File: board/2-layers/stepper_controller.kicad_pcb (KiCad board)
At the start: 4 copper layers, 99 x 46 mm, 124 parts, among them J201 USB_OTG, P103 CONN_4, P105 CONN_4, P107 CONN_4, P201 UART1, P301 12V_Conn, U101 DRV8825, U102 DRV8825, U103 DRV8825, U104 MAX5713/4/5-TSSOP14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

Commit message: footprint cleanup
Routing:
- net +3.3V: track 70.3 -> 73.8 mm, vias 24 -> 25
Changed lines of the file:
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@@
   (general
     (links 339)
-    (no_connects 33)
-    (area 105.189999 86.249999 204.300001 132.400001)
+    (no_connects 31)
+    (area 89.761974 77.9404 204.300001 135.742001)
     (thickness 1.6002)
     (drawings 71)
-    (tracks 677)
+    (tracks 685)
     (zones 0)
     (modules 124)
@@
     (2 GND mixed hide)
     (1 POWER mixed hide)
-    (0 BOTTOM signal hide)
+    (0 BOTTOM signal)
     (16 B.Adhes user)
     (17 F.Adhes user)
@@
   (segment (start 196 95) (end 193.5 95) (width 0.508) (layer BOTTOM) (net 2))
   (segment (start 197 96) (end 196 95) (width 0.508) (layer BOTTOM) (net 2))
+  (segment (start 132.75 94.74956) (end 132.75 94.35) (width 0.2) (layer TOP) (net 3))
+  (via (at 132.8 94.3) (size 0.6096) (layers TOP BOTTOM) (net 3))
+  (segment (start 132.75 94.35) (end 132.8 94.3) (width 0.2) (layer TOP) (net 3))
+  (segment (start 131.11994 94.74956) (end 132.75 94.74956) (width 0.2) (layer TOP) (net 3) (status 400000))
+  (segment (start 132.75 94.74956) (end 134.10444 94.74956) (width 0.2) (layer TOP) (net 3))
+  (segment (start 134.10444 94.74956) (end 134.112 94.742) (width 0.2) (layer TOP) (net 3) (status C00000))
   (segment (start 121.49842 90.9675) (end 121.49842 88.43258) (width 0.2) (layer TOP) (net 3))
   (segment (start 121.49842 88.43258) (end 121.539 88.392) (width 0.2) (layer TOP) (net 3))
@@
   (via (at 155.8 95.5) (size 0.6096) (layers TOP BOTTOM) (net 9))
   (segment (start 155.2986 96.0014) (end 155.8 95.5) (width 0.1524) (layer TOP) (net 9))
-  (segment (start 119.2175 94.24918) (end 125.99918 94.24918) (width 0.1524) (layer TOP) (net 10))
-  (segment (start 147.2528 94.5028) (end 152.003 94.5028) (width 0.1524) (layer TOP) (net 10))
-  (segment (start 147.25 94.5) (end 147.2528 94.5028) (width 0.1524) (layer TOP) (net 10))
-  (via (at 147.25 94.5) (size 0.6096) (layers TOP BOTTOM) (net 10))
-  (segment (start 129.5 94.5) (end 147.25 94.5) (width 0.1524) (layer BOTTOM) (net 10))
-  (segment (start 129.25 94.25) (end 129.5 94.5) (width 0.1524) (layer BOTTOM) (net 10))
-  (via (at 129.25 94.25) (size 0.6096) (layers TOP BOTTOM) (net 10))
-  (segment (start 128 95.5) (end 129.25 94.25) (width 0.1524) (layer TOP) (net 10))
-  (segment (start 127.25 95.5) (end 128 95.5) (width 0.1524) (layer TOP) (net 10))
+  (segment (start 129.5 94.5) (end 130 95) (width 0.1524) (layer BOTTOM) (net 10))
   (segment (start 125.99918 94.24918) (end 127.25 95.5) (width 0.1524) (layer TOP) (net 10))
+  (segment (start 127.25 95.5) (end 128 95.5) (width 0.1524) (layer TOP) (net 10))
+  (segment (start 128 95.5) (end 129.25 94.25) (width 0.1524) (layer TOP) (net 10))
+  (via (at 129.25 94.25) (size 0.6096) (layers TOP BOTTOM) (net 10))
+  (segment (start 129.25 94.25) (end 129.5 94.5) (width 0.1524) (layer BOTTOM) (net 10))
+  (via (at 147.25 94.5) (size 0.6096) (layers TOP BOTTOM) (net 10))
+  (segment (start 147.25 94.5) (end 147.2528 94.5028) (width 0.1524) (layer TOP) (net 10))
+  (segment (start 152.003 94.5028) (end 147.2528 94.5028) (width 0.1524) (layer TOP) (net 10))
+  (segment (start 125.99918 94.24918) (end 119.2175 94.24918) (width 0.1524) (layer TOP) (net 10))
+  (segment (start 146.75 95) (end 147.25 94.5) (width 0.1524) (layer BOTTOM) (net 10))
+  (segment (start 130 95) (end 146.75 95) (width 0.1524) (layer BOTTOM) (net 10))
   (segment (start 119.2175 94.74956) (end 125.49956 94.74956) (width 0.1524) (layer TOP) (net 11))
   (segment (start 158.1 94.4) (end 158.7 94.4) (width 0.1524) (layer BOTTOM) (net 11))

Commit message: blabla
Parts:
- removed P201: UART1, PIN_ARRAY_4x1
- moved C405 6.05 mm to (154.7, 100.1), turned to 270 degrees
- moved C403 3.40 mm to (154.9, 105.1)
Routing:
- net +1.2V: track 9.16 -> 30.2 mm, vias 3 -> 4
- net GND: track 12.1 -> 20.6 mm
- net /VRF_2: track 47.1 -> 49.5 mm
- net /VRF_1: track 17.8 -> 20.1 mm
- net /VRF_0: track 36.0 -> 36.7 mm

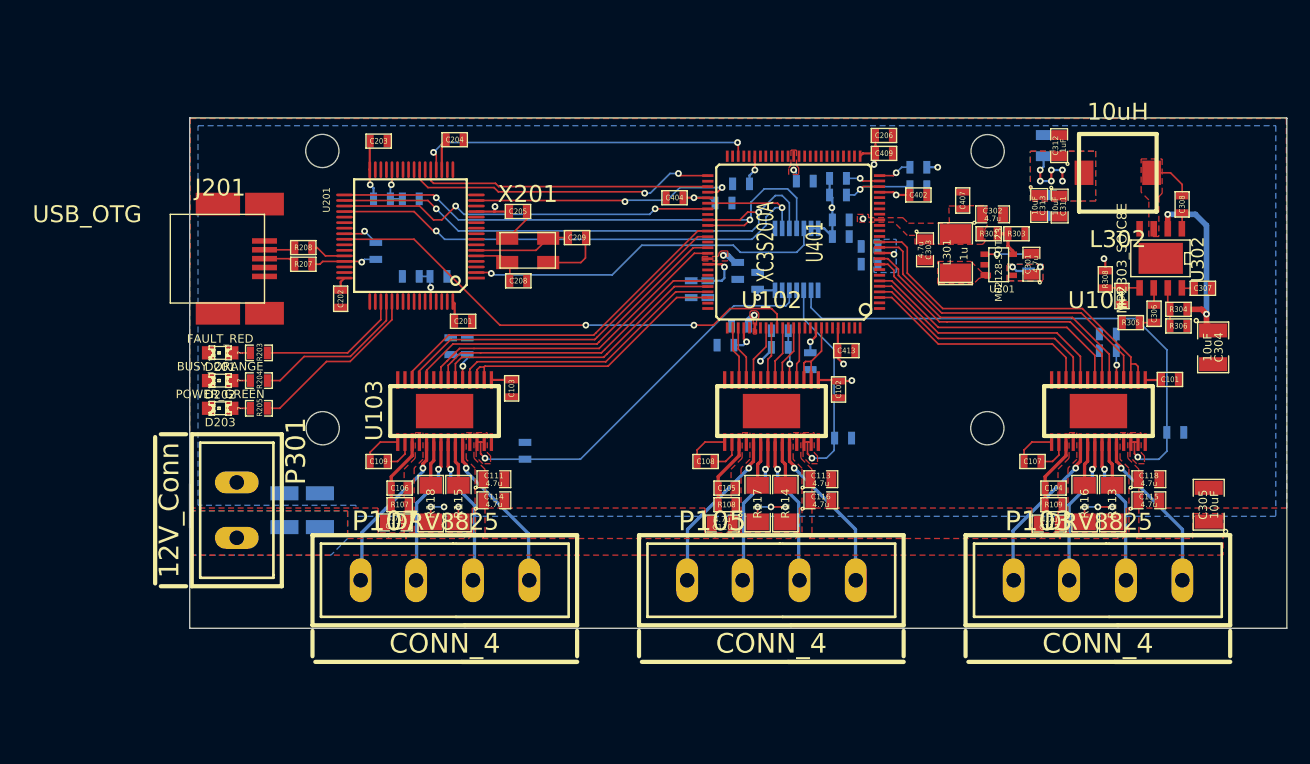
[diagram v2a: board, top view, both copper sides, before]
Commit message: adding mezzanine connector
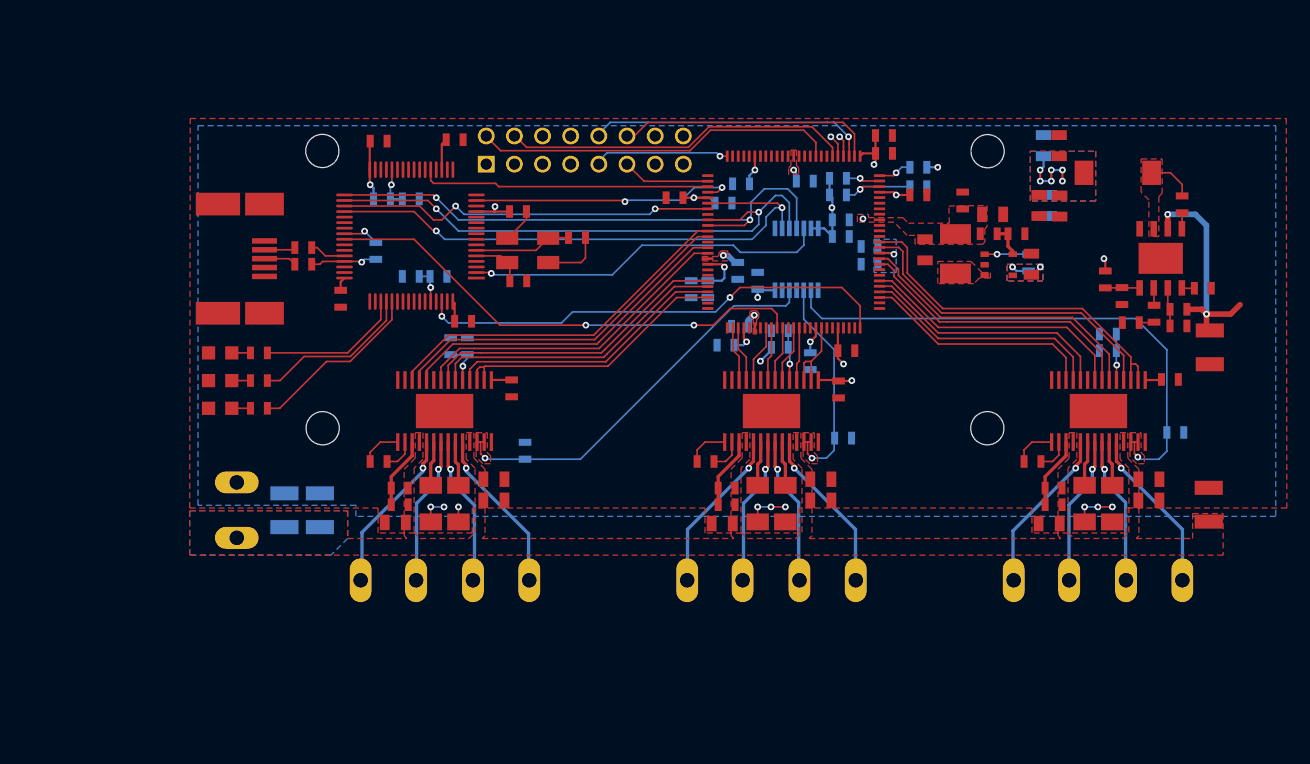
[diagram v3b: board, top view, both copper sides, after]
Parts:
- added P104: CONN_8X2, pin_array_8x2, F.Cu at (140.9, 89.2)
- moved C304 0.30 mm to (197.3, 107.0)
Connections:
- U401 pad 27: (no net) -> /FPGA/L02N
- U401 pad 28: (no net) -> /FPGA/L03P
- U401 pad 29: (no net) -> /FPGA/L03N
- U401 pad 30: (no net) -> /FPGA/L04P
- U401 pad 31: (no net) -> /FPGA/L04N
- U401 pad 34: (no net) -> /FPGA/L06P
- U401 pad 35: (no net) -> /FPGA/L06N
- U401 pad 36: (no net) -> /FPGA/L07P
- U401 pad 37: (no net) -> /FPGA/L07N
- U401 pad 49: (no net) -> /FPGA/L10N
- U401 pad 50: (no net) -> /FPGA/L11P
- U401 pad 52: (no net) -> /FPGA/L11N
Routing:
- net /STM32/FPGA_PROG_B: track 0.00 -> 43.3 mm, vias 0 -> 2
- net /FPGA/L06P: track 0.00 -> 32.8 mm
- net /FPGA/L04N: track 0.00 -> 31.5 mm
- net /STM32/FPGA_INITB: track 30.7 -> 0.00 mm, vias 2 -> 0
- net /FPGA/L04P: track 0.00 -> 29.6 mm, vias 0 -> 1
- net /FPGA/DIN: track 28.2 -> 0.00 mm, vias 2 -> 0
- net /FPGA/L03N: track 0.00 -> 27.3 mm, vias 0 -> 1
- net /FPGA/L03P: track 0.00 -> 25.5 mm, vias 0 -> 1
- net /FPGA/L02N: track 0.00 -> 23.5 mm
- net /FPGA/L11P: track 0.00 -> 12.3 mm, vias 0 -> 1
- net /FPGA/L11N: track 0.00 -> 7.93 mm
- net +12V: track 16.9 -> 20.1 mm
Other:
- board outline removed

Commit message: jtag con & serial
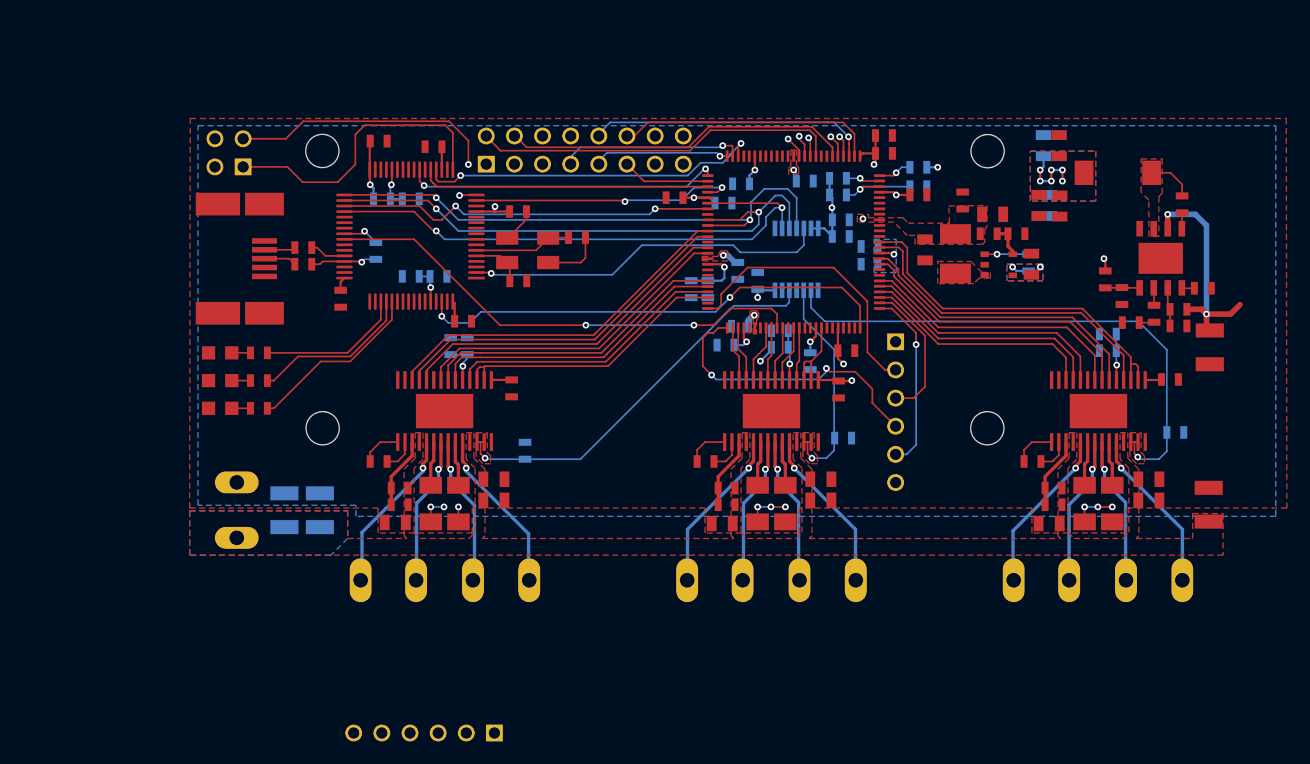
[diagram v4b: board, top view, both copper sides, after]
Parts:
- added P101: JTAG, PIN_ARRAY-6X1, F.Cu at (126.4, 141.8)
- added P102: JTAG, PIN_ARRAY-6X1, F.Cu at (168.9, 112.8)
- added P201: CONN_2X2, PIN_ARRAY_2X2, F.Cu at (108.8, 89.5)
- moved C204 2.01 mm to (127.2, 88.9), turned to 180 degrees
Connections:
- P104 pad 13: +12V -> +3.3V
- P104 pad 14: +3.3V -> GND
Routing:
- net /FPGA/L06N: track 0.00 -> 33.3 mm, vias 0 -> 1
- net /STM32/FPGA_INITB: track 0.00 -> 31.2 mm, vias 0 -> 2
- net /FPGA/L07P: track 0.00 -> 29.1 mm, vias 0 -> 1
- net N-00000127: track 0.00 -> 28.5 mm, vias 0 -> 2
- net /FPGA/DIN: track 0.00 -> 28.4 mm, vias 0 -> 2
- net N-00000115: track 0.00 -> 26.8 mm
- net FPGA_TCK: track 0.00 -> 26.5 mm, vias 0 -> 2
- net /FPGA/L07N: track 0.00 -> 26.4 mm, vias 0 -> 1
- net FPGA_TDO: track 0.00 -> 25.6 mm
- net /FPGA/L10N: track 0.00 -> 16.6 mm, vias 0 -> 1
- net FPGA_TMS: track 0.00 -> 16.5 mm, vias 0 -> 1
- net FPGA_TDI: track 0.00 -> 13.0 mm
- net +3.3V: track 73.8 -> 73.0 mm
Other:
- board text added: "Rx"
- board text added: "TCK"
- board text added: "TDI"
- board text added: "TDO"
- board text added: "TMS"
- board text added: "Tx"

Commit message: routing adc connector + SPI | removed mode selector
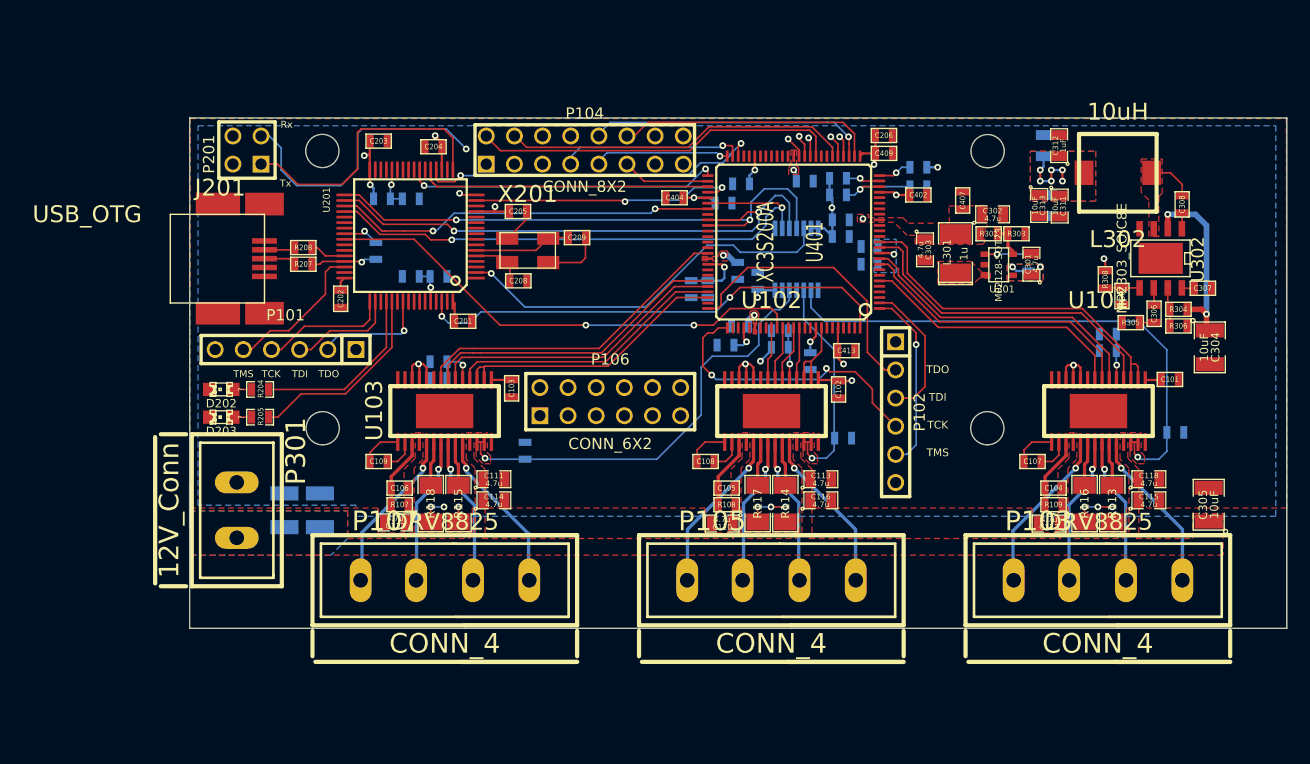
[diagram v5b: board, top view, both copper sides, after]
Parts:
- removed D201: FAULT_RED, LED-0805
- removed R203: ?, SM0603_Resistor
- added P106: CONN_6X2, pin_array_6x2, F.Cu at (143.2, 111.9)
- moved P101 36.8 mm to (113.9, 107.2)
- moved R102 3.89 mm to (127.7, 109.8), turned to 0 degrees
- moved R101 1.78 mm to (127.7, 108.3), turned to 180 degrees
- moved P201 1.64 mm to (110.4, 89.2)
- moved D202 0.81 mm to (108.1, 110.8)
- moved D203 0.81 mm to (108.1, 113.3)
- moved R204 0.81 mm to (111.6, 110.8)
- moved R205 0.81 mm to (111.6, 113.3)
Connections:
- U101 pad 24: /FPGA/M2_MODE0 -> +3.3V
- U101 pad 25: /FPGA/M2_MODE1 -> +3.3V
- U101 pad 26: /FPGA/M2_MODE2 -> +3.3V
- U102 pad 24: /FPGA/M1_MODE0 -> +3.3V
- U102 pad 25: /FPGA/M1_MODE1 -> +3.3V
- U102 pad 26: /FPGA/M1_MODE2 -> +3.3V
- U103 pad 24: /FPGA/M0_MODE0 -> +3.3V
- U103 pad 25: /FPGA/M0_MODE1 -> +3.3V
- U103 pad 26: /FPGA/M0_MODE2 -> +3.3V
- U201 pad 51: N-00000105 -> (no net)
- U401 pad 3: /FPGA/M2_MODE2 -> (no net)
- U401 pad 4: /FPGA/M2_MODE1 -> (no net)
- U401 pad 5: /FPGA/M2_MODE0 -> (no net)
- U401 pad 61: /FPGA/M0_MODE2 -> (no net)
- U401 pad 62: /FPGA/M0_MODE1 -> (no net)
- U401 pad 64: /FPGA/M0_MODE0 -> (no net)
- U401 pad 77: /FPGA/M1_MODE2 -> (no net)
- U401 pad 78: /FPGA/M1_MODE1 -> (no net)
- U401 pad 83: /FPGA/M1_MODE0 -> (no net)
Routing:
- net /FPGA/M0_MODE2: track 32.7 -> 0.00 mm
- net /FPGA/M0_MODE1: track 31.9 -> 0.00 mm
- net /FPGA/M0_MODE0: track 30.8 -> 0.00 mm
- net /FPGA/M2_MODE0: track 22.9 -> 0.00 mm
- net /FPGA/M2_MODE1: track 22.0 -> 0.00 mm
- net /FPGA/M2_MODE2: track 21.1 -> 0.00 mm
- net +3.3V: track 73.0 -> 90.6 mm, vias 25 -> 30
- net EXT_JTAG_TMS: track 0.00 -> 13.4 mm
- net N-00000105: track 13.1 -> 0.00 mm
- net EXT_JTAG_TCK: track 0.00 -> 11.6 mm
- net EXT_JTAG_TDO: track 0.00 -> 10.4 mm, vias 0 -> 1
- net EXT_JTAG_TDI: track 0.00 -> 9.75 mm
- net /FPGA/M1_MODE0: track 5.17 -> 0.00 mm
- net /FPGA/M1_MODE1: track 5.01 -> 0.00 mm
- net /FPGA/M1_MODE2: track 4.94 -> 0.00 mm
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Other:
- board outline added: 99 x 46 mm

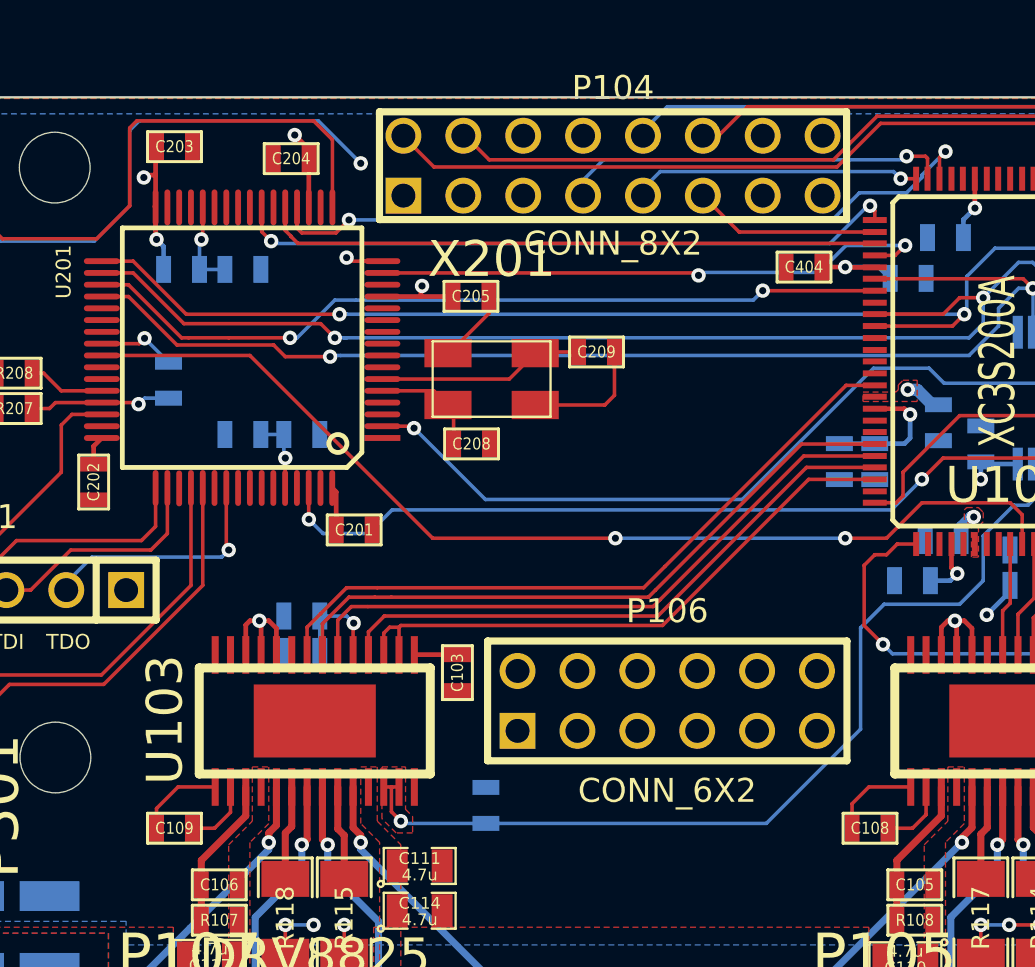
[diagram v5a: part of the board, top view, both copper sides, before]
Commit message: routing adc input
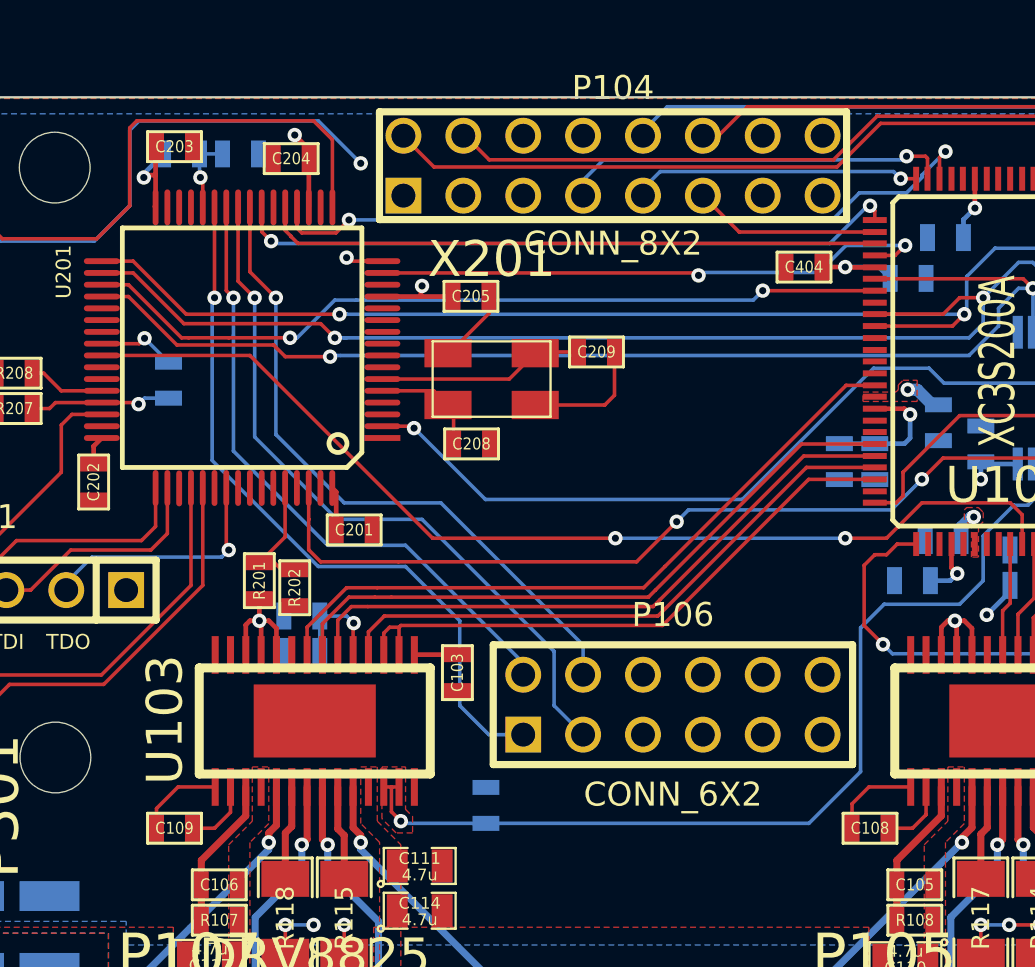
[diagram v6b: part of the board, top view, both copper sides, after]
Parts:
- R201, R202: moved to F.Cu
- moved R202 6.51 mm to (127.4, 107.1), turned to 270 degrees
- moved R201 6.24 mm to (125.9, 106.8), turned to 90 degrees
- moved R210 4.90 mm to (125.1, 88.7)
- moved R209 4.90 mm to (122.6, 88.7)
- moved P106 0.29 mm to (143.4, 112.1)
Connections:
- P106 pad 1: (no net) -> /STM32/PB1_ADC12IN9
- P106 pad 11: (no net) -> GND
- P106 pad 12: (no net) -> GND
- P106 pad 2: (no net) -> /STM32/PB0_ADC12IN8
- P106 pad 3: (no net) -> /STM32/PC5_ADC12IN15
- P106 pad 4: (no net) -> /STM32/PC4_ADC12IN14
- P106 pad 9: (no net) -> +3.3V
- U201 pad 24: (no net) -> /STM32/PC4_ADC12IN14
- U201 pad 25: (no net) -> /STM32/PC5_ADC12IN15
- U201 pad 26: (no net) -> /STM32/PB0_ADC12IN8
- U201 pad 27: (no net) -> /STM32/PB1_ADC12IN9
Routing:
- net /STM32/PB1_ADC12IN9: track 0.00 -> 30.9 mm, vias 0 -> 1
- net /STM32/PC5_ADC12IN15: track 0.00 -> 30.5 mm, vias 0 -> 1
- net /STM32/PC4_ADC12IN14: track 0.00 -> 28.1 mm, vias 0 -> 1
- net /STM32/PB0_ADC12IN8: track 0.00 -> 27.0 mm, vias 0 -> 1
- net /STM32/BOOT0: track 3.27 -> 5.24 mm, vias 1 -> 0
- net /STM32/FPGA_PROG_B: track 43.3 -> 45.1 mm
- net /VRF_0: track 40.2 -> 41.3 mm
- net +3.3V: track 90.6 -> 90.2 mm, vias 30 -> 29

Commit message: pouet
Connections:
- P106 pad 10: (no net) -> /STM32/PC15
- P106 pad 5: (no net) -> /FPGA/COM_MISO
- P106 pad 6: (no net) -> /FPGA/COM_CLK
- P106 pad 7: (no net) -> /FPGA/COM_MOSI
- P106 pad 8: (no net) -> /STM32/PC14
- U201 pad 3: (no net) -> /STM32/PC14
- U201 pad 4: (no net) -> /STM32/PC15
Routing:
- net /FPGA/COM_MISO: track 34.5 -> 61.0 mm
- net /FPGA/COM_MOSI: track 50.9 -> 76.8 mm
- net /STM32/PC15: track 0.00 -> 25.8 mm, vias 0 -> 1
- net /FPGA/COM_CLK: track 50.8 -> 75.1 mm
- net /STM32/PC14: track 0.00 -> 22.2 mm, vias 0 -> 1
- net +3.3V: track 90.2 -> 104.5 mm, vias 29 -> 31
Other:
- board outline removed
